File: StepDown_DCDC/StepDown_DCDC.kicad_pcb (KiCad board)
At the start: 2 copper layers, 40.6 x 30.5 mm, 12 parts, among them J1 IN, J2 OUT, U1 LM2596S-5

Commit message: Update
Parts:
- D1: value 1N5822 -> 1N5824; footprint Diode_SMD:D_MELF -> Diode_SMD:D_SMA
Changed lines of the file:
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@@
       (outputformat 1)
       (mirror false)
-      (drillshape 1)
+      (drillshape 0)
       (scaleselection 1)
-      (outputdirectory "")
+      (outputdirectory "Assembly/Gerber/")
     )
   )
@@
     )
   )
-  (footprint "Diode_SMD:D_MELF" (layer "F.Cu")
+  (footprint "Diode_SMD:D_SMA" (layer "F.Cu")
     (at 73.66 85.344)
-    (descr "Diode, MELF,,")
-    (tags "Diode MELF ")
-    (property "Sheetfile" "StepDown_DCDC.kicad_sch")
-    (property "Sheetname" "")
-    (attr smd)
-    (fp_text reference "D1" (at 0 2.286) (layer "F.SilkS")
-      (effects (font (size 1 1) (thickness 0.15)))
-    )
-    (fp_text value "1N5822" (at -0.25 2.5) (layer "F.Fab")
+    (descr "Diode SMA (DO-214AC)")
+    (tags "Diode SMA (DO-214AC)")
+    (property "Sheetfile" "StepDown_DCDC.kicad_sch")
+    (property "Sheetname" "")
+    (attr smd)
+    (fp_text reference "D1" (at 0 2.54) (layer "F.SilkS")
+      (effects (font (size 1 1) (thickness 0.15)))
+    )
+    (fp_text value "1N5824" (at 0 2.6) (layer "F.Fab")
       (effects (font (size 1 1) (thickness 0.15)))
     )
@@
       (effects (font (size 1 1) (thickness 0.15)))
     )
-    (fp_line (start -3.3 -1.5) (end -3.3 1.5) (layer "F.SilkS") (width 0.12))
-    (fp_line (start 2.4 -1.5) (end -3.3 -1.5) (layer "F.SilkS") (width 0.12))
-    (fp_line (start -3.3 1.5) (end 2.4 1.5) (layer "F.SilkS") (width 0.12))
-    (fp_line (start -3.4 1.6) (end -3.4 -1.6) (layer "F.CrtYd") (width 0.05))
-    (fp_line (start 3.4 1.6) (end -3.4 1.6) (layer "F.CrtYd") (width 0.05))
-    (fp_line (start -3.4 -1.6) (end 3.4 -1.6) (layer "F.CrtYd") (width 0.05))
-    (fp_line (start 3.4 -1.6) (end 3.4 1.6) (layer "F.CrtYd") (width 0.05))
+    (fp_line (start -3.4 -1.65) (end 2 -1.65) (layer "F.SilkS") (width 0.12))
+    (fp_line (start -3.4 -1.65) (end -3.4 1.65) (layer "F.SilkS") (width 0.12))
+    (fp_line (start -3.4 1.65) (end 2 1.65) (layer "F.SilkS") (width 0.12))
+    (fp_line (start 3.5 1.75) (end -3.5 1.75) (layer "F.CrtYd") (width 0.05))
+    (fp_line (start 3.5 -1.75) (end 3.5 1.75) (layer "F.CrtYd") (width 0.05))
+    (fp_line (start -3.5 1.75) (end -3.5 -1.75) (layer "F.CrtYd") (width 0.05))
+    (fp_line (start -3.5 -1.75) (end 3.5 -1.75) (layer "F.CrtYd") (width 0.05))
+    (fp_line (start 0.50118 0.00102) (end 1.4994 0.00102) (layer "F.Fab") (width 0.1))
+    (fp_line (start -0.64944 0.00102) (end 0.50118 -0.79908) (layer "F.Fab") (width 0.1))
+    (fp_line (start -0.64944 -0.79908) (end -0.64944 0.80112) (layer "F.Fab") (width 0.1))
+    (fp_line (start 2.3 1.5) (end -2.3 1.5) (layer "F.Fab") (width 0.1))
     (fp_line (start -0.64944 0.00102) (end -1.55114 0.00102) (layer "F.Fab") (width 0.1))
-    (fp_line (start -2.6 -1.3) (end -2.6 1.3) (layer "F.Fab") (width 0.1))
-    (fp_line (start 2.6 1.3) (end 2.6 -1.3) (layer "F.Fab") (width 0.1))
     (fp_line (start -0.64944 0.00102) (end 0.50118 0.75032) (layer "F.Fab") (width 0.1))
-    (fp_line (start -0.64944 -0.79908) (end -0.64944 0.80112) (layer "F.Fab") (width 0.1))
-    (fp_line (start 2.6 -1.3) (end -2.6 -1.3) (layer "F.Fab") (width 0.1))
-    (fp_line (start -2.6 1.3) (end 2.6 1.3) (layer "F.Fab") (width 0.1))
-    (fp_line (start -0.64944 0.00102) (end 0.50118 -0.79908) (layer "F.Fab") (width 0.1))
-    (fp_line (start 0.50118 0.00102) (end 1.4994 0.00102) (layer "F.Fab") (width 0.1))
+    (fp_line (start -2.3 1.5) (end -2.3 -1.5) (layer "F.Fab") (width 0.1))
     (fp_line (start 0.50118 0.75032) (end 0.50118 -0.79908) (layer "F.Fab") (width 0.1))
-    (pad "1" smd rect locked (at -2.4 0) (size 1.5 2.7) (layers "F.Cu" "F.Paste" "F.Mask")
+    (fp_line (start 2.3 -1.5) (end -2.3 -1.5) (layer "F.Fab") (width 0.1))
+    (fp_line (start 2.3 -1.5) (end 2.3 1.5) (layer "F.Fab") (width 0.1))
+    (pad "1" smd rect locked (at -2 0) (size 2.5 1.8) (layers "F.Cu" "F.Paste" "F.Mask")
       (net 5 "Net-(D1-Pad1)") (pinfunction "K") (pintype "passive"))
-    (pad "2" smd rect locked (at 2.4 0) (size 1.5 2.7) (layers "F.Cu" "F.Paste" "F.Mask")
+    (pad "2" smd rect locked (at 2 0) (size 2.5 1.8) (layers "F.Cu" "F.Paste" "F.Mask")
       (net 2 "GND") (pinfunction "A") (pintype "passive"))
-    (model "${KICAD6_3DMODEL_DIR}/Diode_SMD.3dshapes/D_MELF.wrl"
+    (model "${KICAD6_3DMODEL_DIR}/Diode_SMD.3dshapes/D_SMA.wrl"
       (offset (xyz 0 0 0))
       (scale (xyz 1 1 1))
@@
     (fp_line (start 1 0.625) (end -1 0.625) (layer "F.Fab") (width 0.1))
     (fp_line (start -1 0.625) (end -1 -0.625) (layer "F.Fab") (width 0.1))
-    (pad "1" smd roundrect locked (at -0.9125 0 180) (size 1.025 1.4) (layers "F.Cu" "F.Paste" "F.Mask") (roundrect_rratio 0.243902)
+    (pad "1" smd roundrect locked (at -0.9125 0 180) (size 1.025 1.4) (layers "F.Cu" "F.Paste" "F.Mask") (roundrect_rratio 0.243902439)
       (net 4 "Net-(C3-Pad2)") (pintype "passive"))
-    (pad "2" smd roundrect locked (at 0.9125 0 180) (size 1.025 1.4) (layers "F.Cu" "F.Paste" "F.Mask") (roundrect_rratio 0.243902)
+    (pad "2" smd roundrect locked (at 0.9125 0 180) (size 1.025 1.4) (layers "F.Cu" "F.Paste" "F.Mask") (roundrect_rratio 0.243902439)
       (net 2 "GND") (pintype "passive"))
     (model "${KICAD6_3DMODEL_DIR}/Resistor_SMD.3dshapes/R_0805_2012Metric.wrl"
@@
     (fp_line (start -1.27 -0.5) (end -0.562893 0) (layer "F.Fab") (width 0.1))
     (fp_line (start -1.27 -2.92) (end -1.27 2.88) (layer "F.Fab") (width 0.1))
-    (pad "1" thru_hole roundrect locked (at 0 0) (size 1.74 2.19) (drill 1.19) (layers *.Cu *.Mask) (roundrect_rratio 0.143678)
+    (pad "1" thru_hole roundrect locked (at 0 0) (size 1.74 2.19) (drill 1.19) (layers *.Cu *.Mask) (roundrect_rratio 0.1436781609)
       (net 2 "GND") (pinfunction "Pin_1") (pintype "passive"))
     (pad "2" thru_hole oval locked (at 2.54 0) (size 1.74 2.19) (drill 1.19) (layers *.Cu *.Mask)
@@
     (fp_line (start -1 -0.625) (end 1 -0.625) (layer "F.Fab") (width 0.1))
     (fp_line (start 1 0.625) (end -1 0.625) (layer "F.Fab") (width 0.1))
-    (pad "1" smd roundrect locked (at -0.9125 0 180) (size 1.025 1.4) (layers "F.Cu" "F.Paste" "F.Mask") (roundrect_rratio 0.243902)
+    (pad "1" smd roundrect locked (at -0.9125 0 180) (size 1.025 1.4) (layers "F.Cu" "F.Paste" "F.Mask") (roundrect_rratio 0.243902439)
       (net 6 "Net-(D2-Pad2)") (pintype "passive"))
-    (pad "2" smd roundrect locked (at 0.9125 0 180) (size 1.025 1.4) (layers "F.Cu" "F.Paste" "F.Mask") (roundrect_rratio 0.243902)
+    (pad "2" smd roundrect locked (at 0.9125 0 180) (size 1.025 1.4) (layers "F.Cu" "F.Paste" "F.Mask") (roundrect_rratio 0.243902439)
       (net 2 "GND") (pintype "passive"))
     (model "${KICAD6_3DMODEL_DIR}/Resistor_SMD.3dshapes/R_0805_2012Metric.wrl"
@@
     (fp_line (start -1.27 -2.92) (end -1.27 2.88) (layer "F.Fab") (width 0.1))
     (fp_line (start -1.27 -0.5) (end -0.562893 0) (layer "F.Fab") (width 0.1))
-    (pad "1" thru_hole roundrect locked (at 0 0) (size 1.74 2.19) (drill 1.19) (layers *.Cu *.Mask) (roundrect_rratio 0.143678)
+    (pad "1" thru_hole roundrect locked (at 0 0) (size 1.74 2.19) (drill 1.19) (layers *.Cu *.Mask) (roundrect_rratio 0.1436781609)
       (net 2 "GND") (pinfunction "Pin_1") (pintype "passive"))
     (pad "2" thru_hole oval locked (at 2.54 0) (size 1.74 2.19) (drill 1.19) (layers *.Cu *.Mask)
@@
     (fp_line (start -1 0.625) (end -1 -0.625) (layer "F.Fab") (width 0.1))
     (fp_line (start 1 0.625) (end -1 0.625) (layer "F.Fab") (width 0.1))
-    (pad "1" smd roundrect locked (at -0.9125 0 180) (size 1.025 1.4) (layers "F.Cu" "F.Paste" "F.Mask") (roundrect_rratio 0.243902)
+    (pad "1" smd roundrect locked (at -0.9125 0 180) (size 1.025 1.4) (layers "F.Cu" "F.Paste" "F.Mask") (roundrect_rratio 0.243902439)
       (net 3 "+5V") (pintype "passive"))
-    (pad "2" smd roundrect locked (at 0.9125 0 180) (size 1.025 1.4) (layers "F.Cu" "F.Paste" "F.Mask") (roundrect_rratio 0.243902)
+    (pad "2" smd roundrect locked (at 0.9125 0 180) (size 1.025 1.4) (layers "F.Cu" "F.Paste" "F.Mask") (roundrect_rratio 0.243902439)
       (net 4 "Net-(C3-Pad2)") (pintype "passive"))
     (model "${KICAD6_3DMODEL_DIR}/Resistor_SMD.3dshapes/R_0805_2012Metric.wrl"
@@
   (segment (start 78.693 84.582) (end 78.693 89.107) (width 1) (layer "F.Cu") (net 4))
   (segment (start 77.665 80.385) (end 77.665 83.554) (width 1) (layer "F.Cu") (net 4))
-  (segment (start 74.265 83.685) (end 72.606 85.344) (width 1) (layer "F.Cu") (net 5))
-  (segment (start 64.262 82.21) (end 68.126 82.21) (width 1) (layer "F.Cu") (net 5))
-  (segment (start 74.265 80.385) (end 74.265 83.685) (width 1) (layer "F.Cu") (net 5))
-  (segment (start 72.606 85.344) (end 71.26 85.344) (width 1) (layer "F.Cu") (net 5))
-  (segment (start 68.126 82.21) (end 71.26 85.344) (width 1) (layer "F.Cu") (net 5))
+  (segment (start 68.126 82.21) (end 64.262 82.21) (width 1) (layer "F.Cu") (net 5))
+  (segment (start 74.265 83.215) (end 72.136 85.344) (width 1) (layer "F.Cu") (net 5))
+  (segment (start 74.265 80.385) (end 74.265 83.215) (width 1) (layer "F.Cu") (net 5))
+  (segment (start 71.26 85.344) (end 68.126 82.21) (width 1) (layer "F.Cu") (net 5))
+  (segment (start 72.136 85.344) (end 71.26 85.344) (width 1) (layer "F.Cu") (net 5))
   (segment (start 92.3775 91.44) (end 92.3775 88.417) (width 1) (layer "F.Cu") (net 6))
   (segment (start 92.3775 88.417) (end 92.3525 88.392) (width 1) (layer "F.Cu") (net 6))

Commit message: Add libraries
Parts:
- removed C3: 15nF, Capacitor_SMD:C_0805_2012Metric
- removed R1: 1K, Resistor_SMD:R_0805_2012Metric
- removed R2: 3K, Resistor_SMD:R_0805_2012Metric
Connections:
- U1 pad 4: Net-(C3-Pad2) -> +5V
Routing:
- net Net-(C3-Pad2): track 9.21 -> 0.00 mm
- net +5V: track 58.8 -> 65.0 mm
- net +12V: track 42.3 -> 43.7 mm
- net GND: track 35.0 -> 33.6 mm

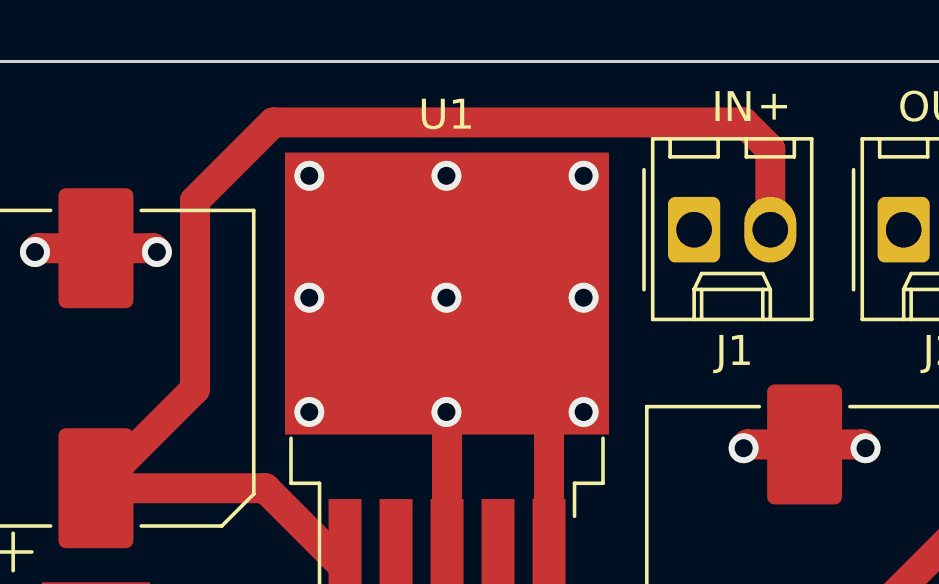
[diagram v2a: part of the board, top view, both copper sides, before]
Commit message: Restructure libraries
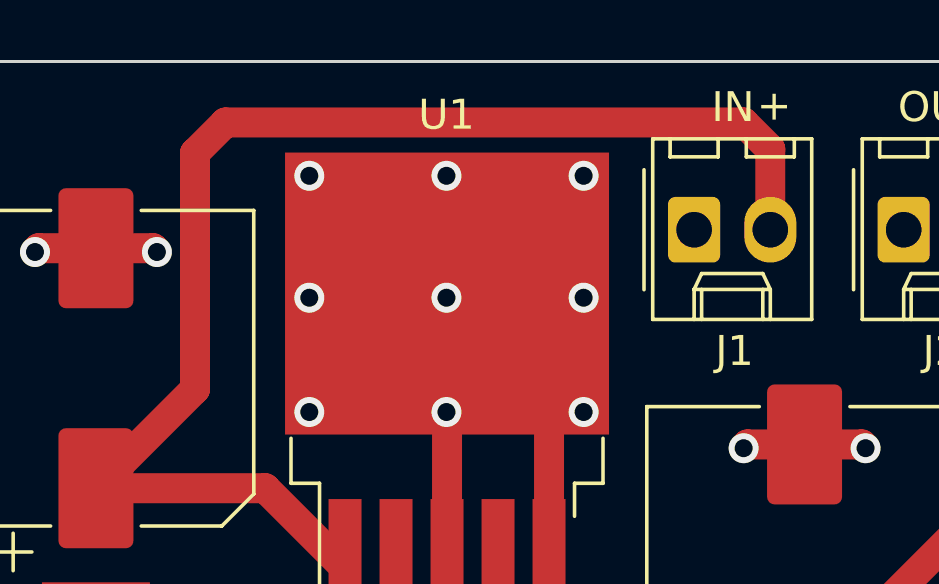
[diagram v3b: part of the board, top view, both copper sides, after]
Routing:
- net +12V: track 43.7 -> 44.6 mm
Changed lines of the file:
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@@
     (effects (font (size 1 1) (thickness 0.15)))
   )
-  (segment (start 67.564 68.136978) (end 67.564 74.422) (width 1) (layer "F.Cu") (net 1))
+  (segment (start 85.852 65.532) (end 68.58 65.532) (width 1) (layer "F.Cu") (net 1))
   (segment (start 69.904 77.724) (end 72.565 80.385) (width 1) (layer "F.Cu") (net 1))
+  (segment (start 67.564 66.548) (end 67.564 74.422) (width 1) (layer "F.Cu") (net 1))
+  (segment (start 68.58 65.532) (end 67.564 66.548) (width 1) (layer "F.Cu") (net 1))
+  (segment (start 64.262 77.724) (end 69.904 77.724) (width 1) (layer "F.Cu") (net 1))
   (segment (start 86.741 66.421) (end 85.852 65.532) (width 1) (layer "F.Cu") (net 1))
-  (segment (start 70.168978 65.532) (end 67.564 68.136978) (width 1) (layer "F.Cu") (net 1))
-  (segment (start 64.262 77.724) (end 69.904 77.724) (width 1) (layer "F.Cu") (net 1))
   (segment (start 67.564 74.422) (end 64.262 77.724) (width 1) (layer "F.Cu") (net 1))
   (segment (start 86.741 69.108) (end 86.741 66.421) (width 1) (layer "F.Cu") (net 1))
-  (segment (start 85.852 65.532) (end 70.168978 65.532) (width 1) (layer "F.Cu") (net 1))
   (segment (start 85.978 76.264) (end 85.852 76.39) (width 1) (layer "F.Cu") (net 2))
   (segment (start 64.262 69.724) (end 62.356 69.724) (width 1) (layer "F.Cu") (net 2))
